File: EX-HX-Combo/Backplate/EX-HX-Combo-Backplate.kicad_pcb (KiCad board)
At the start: 2 copper layers, 91.5 x 134.5 mm, 5 parts

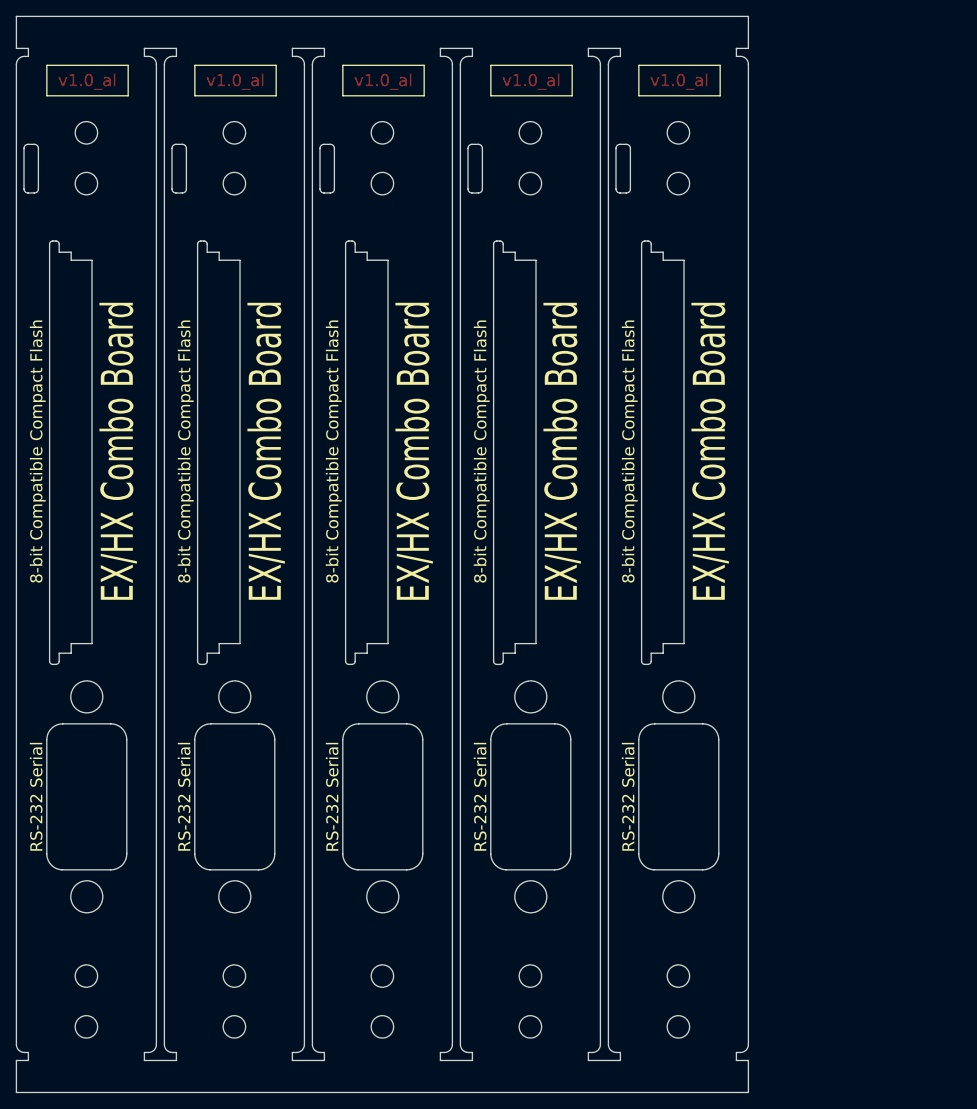
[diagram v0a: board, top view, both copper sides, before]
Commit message: Alternative EX-HX-Combo-Backpate designed for Aluminium manufacture.
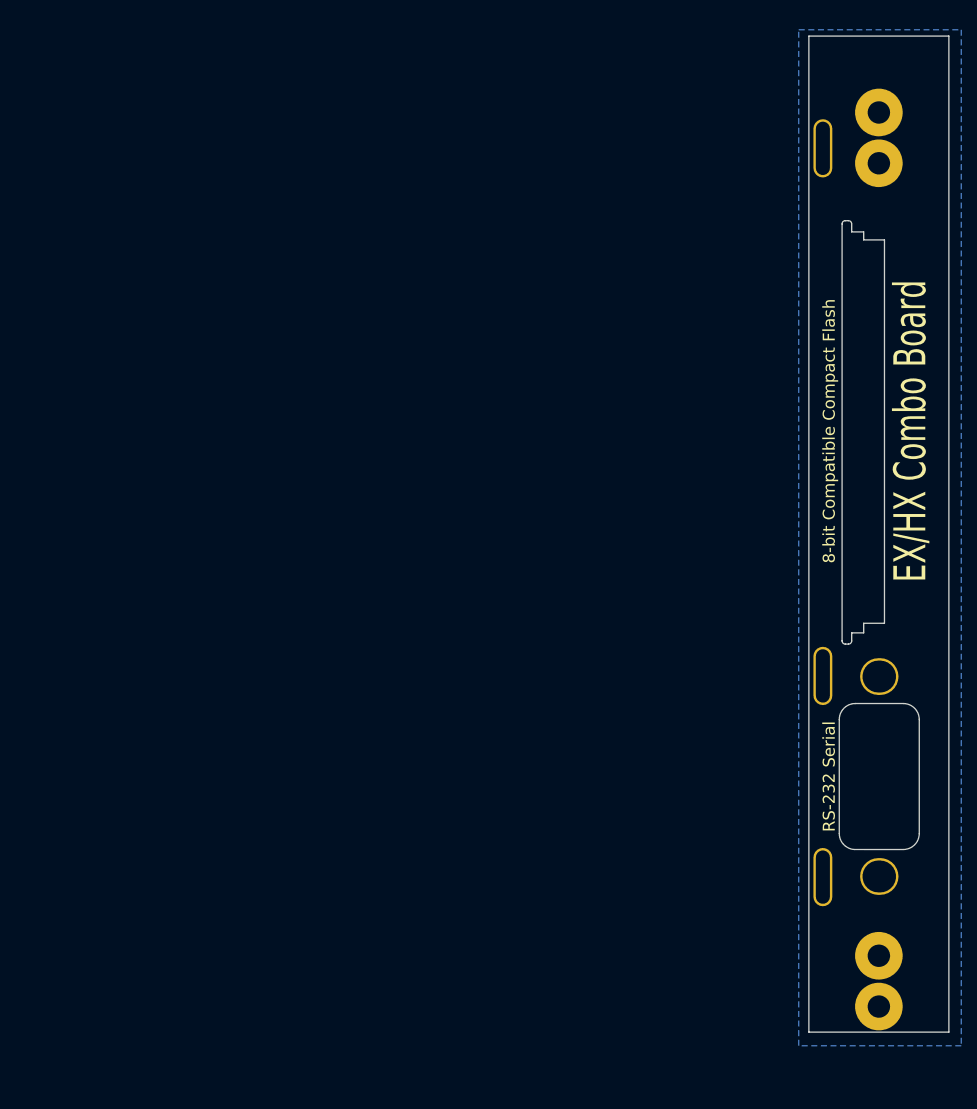
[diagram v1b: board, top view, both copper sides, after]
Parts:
- removed the H1 at (230.2, 122.6)
- removed the H1 at (211.7, 122.6)
- removed the H1 at (193.2, 122.6)
- removed the H1 at (174.7, 122.6)
- removed the H1 at (156.2, 122.6)
- added H1: MountingHole_Pad, MountingHole:MountingHole_3.5mm_Pad, F.Cu at (261.5, 37.0)
- added H2: MountingHole_Pad, MountingHole:MountingHole_3.5mm_Pad, F.Cu at (261.5, 43.4)
- added H3: MountingHole_Pad, MountingHole:MountingHole_3.5mm_Pad, F.Cu at (261.5, 142.4)
- added H4: MountingHole_Pad, MountingHole:MountingHole_3.5mm_Pad, F.Cu at (261.5, 148.8)
- added H5: AlignmentHole_Pad, 00Custom:AlignmentHole, F.Cu at (254.5, 132.6)
- added H6: AlignmentHole_Pad, 00Custom:AlignmentHole, F.Cu at (254.5, 107.4)
- added H7: AlignmentHole_Pad, 00Custom:AlignmentHole, F.Cu at (254.5, 41.5)
- added H8: DB-9 Faceplate, 00Custom:DB9_Face, F.Cu at (255.3, 120.0)
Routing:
- added copper zone on B.Cu, net GND
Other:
- board size 91.5 x 134.5 mm -> 17.5 x 124.5 mm
- board text added: "Copyright (C) 2021 Titanium Studios Pty Ltd Creative Commons Attribution-ShareAlike 4.0 International https://github.com/JayesonLS/ISA-Cards"
- board text added: "JLCJLCJLCJLC"
- board text added: "Maxium recommended length. This will almost reach the ROM when a SmartWatch is fitted in an HX. Tall components this far back will hit the top of the case when the board is in the top position."
- board text removed: "Align center line on board and faceplate before soldering to faceplate"
- board text removed: "v1.0_al"

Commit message: EX-HX-Combo: WIP on backplate refinements.
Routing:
- added copper zone on F.Cu, net GND
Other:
- board size 17.5 x 124.5 mm -> 17.5 x 120.2 mm
- board text added: "COM1"
- board text added: "EX/HX Combo"
- board text added: "v1.1"
- board text removed: "EX/HX Combo Board"
- board text removed: "JLCJLCJLCJLC"
- board text removed: "RS-232 Serial"
